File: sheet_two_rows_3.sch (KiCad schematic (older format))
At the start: 70 parts, among them U1 SN74HC595N_6_b, U2 SN74HC595N_6_g, U3 SN74HC595N_6_r, U4 SN74HC595N_7_b, U5 SN74HC595N_7_g, U6 SN74HC595N_7_r

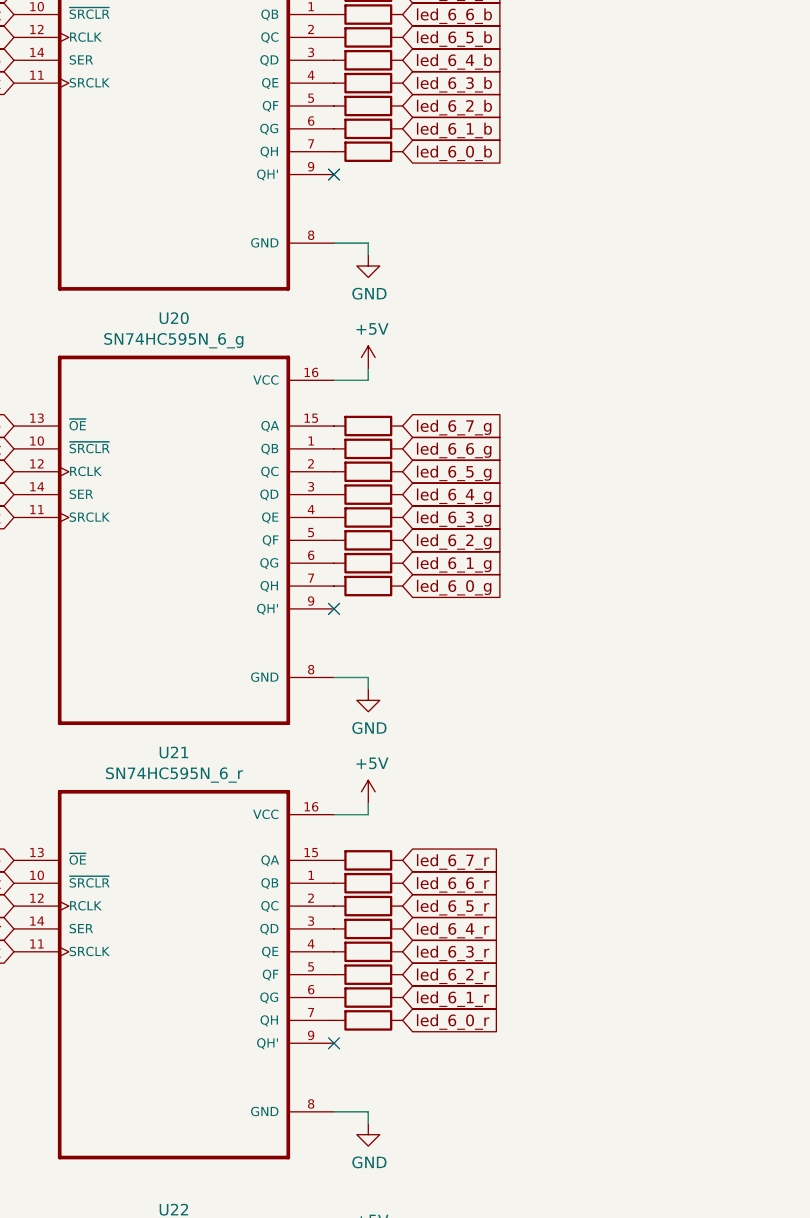
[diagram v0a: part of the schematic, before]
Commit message: fix 8th rows's green conns
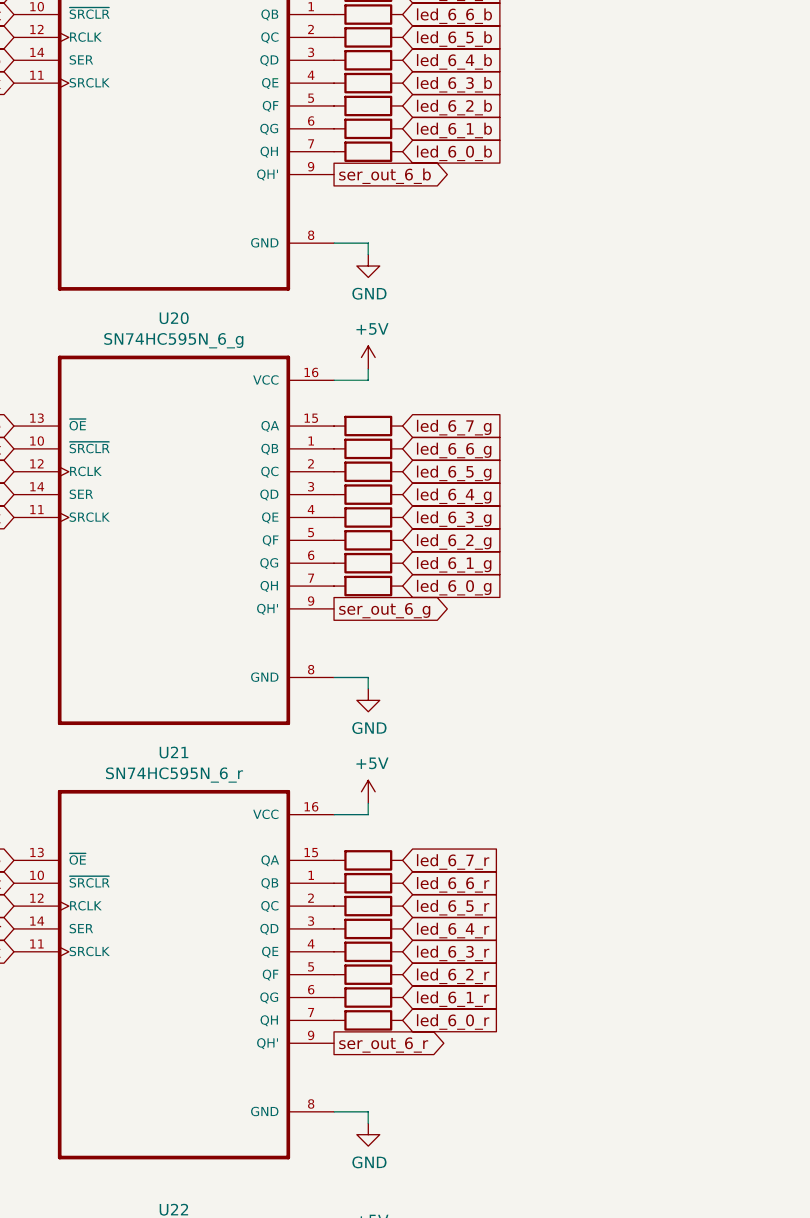
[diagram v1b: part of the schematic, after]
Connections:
- net ser_out_6_b: now also U1.9 (QH')
- net ser_out_6_g: now also U2.9 (QH')
- net ser_out_6_r: now also U3.9 (QH')
- no-connect marks 6 -> 3
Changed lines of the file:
@@
 Text GLabel 1550 8650 0    50   Input ~ 0
 ser_out_6_b
-NoConn ~ 2950 3350
-NoConn ~ 2950 5250
-NoConn ~ 2950 7150
 NoConn ~ 2950 9150
 NoConn ~ 2950 11050
 NoConn ~ 2950 12950
+Text GLabel 2950 3350 2    50   Output ~ 0
+ser_out_6_b
+Text GLabel 2950 5250 2    50   Output ~ 0
+ser_out_6_g
+Text GLabel 2950 7150 2    50   Output ~ 0
+ser_out_6_r
 $EndSCHEMATC
